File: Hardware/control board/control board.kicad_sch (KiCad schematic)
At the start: 9 parts, among them J1 Conn_01x03_Pin, J2 Conn_01x03_Pin, J3 Conn_01x03_Pin, J4 Conn_01x03_Pin, J5 Conn_01x03_Pin, J6 Conn_01x03_Pin, J7 Conn_01x03_Pin, J8 Conn_01x03_Pin

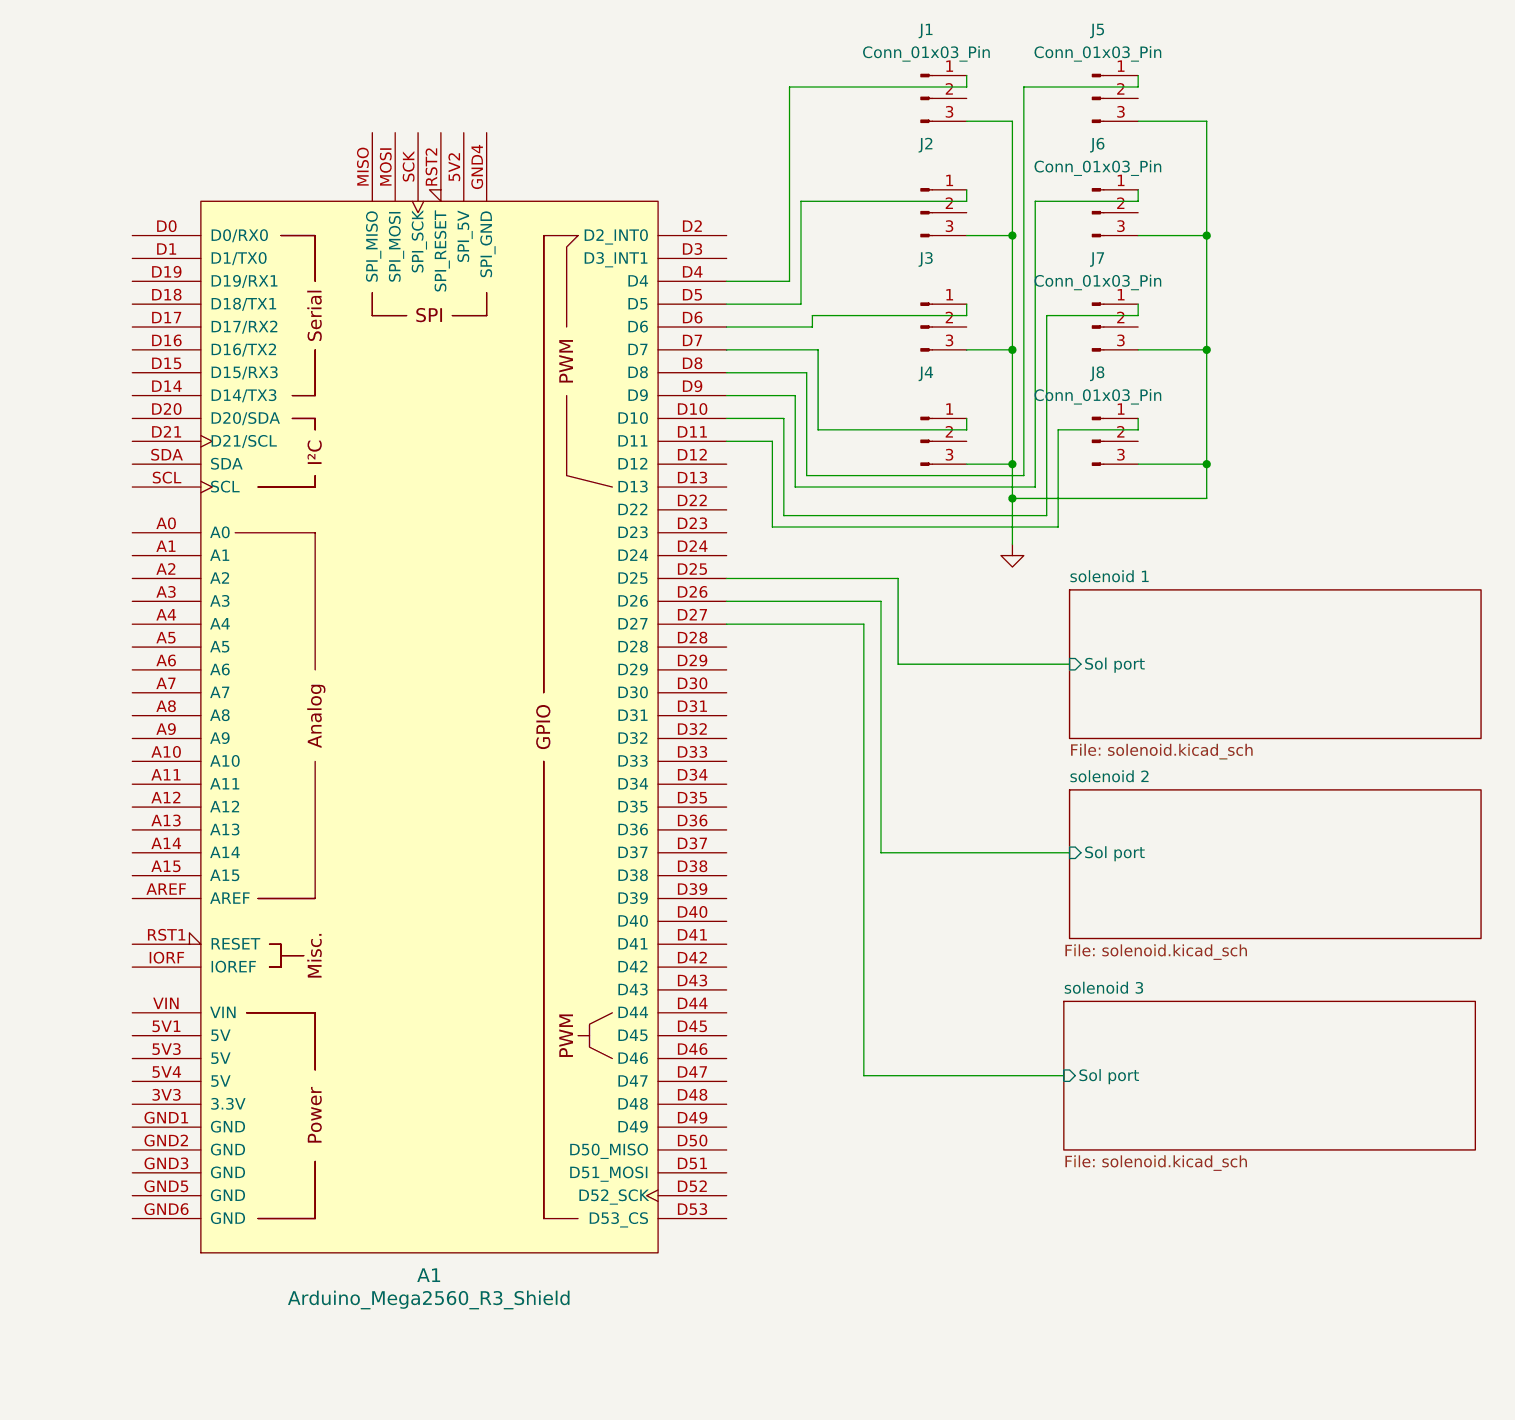
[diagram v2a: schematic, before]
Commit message: updated resistor values for 14.8 V battery
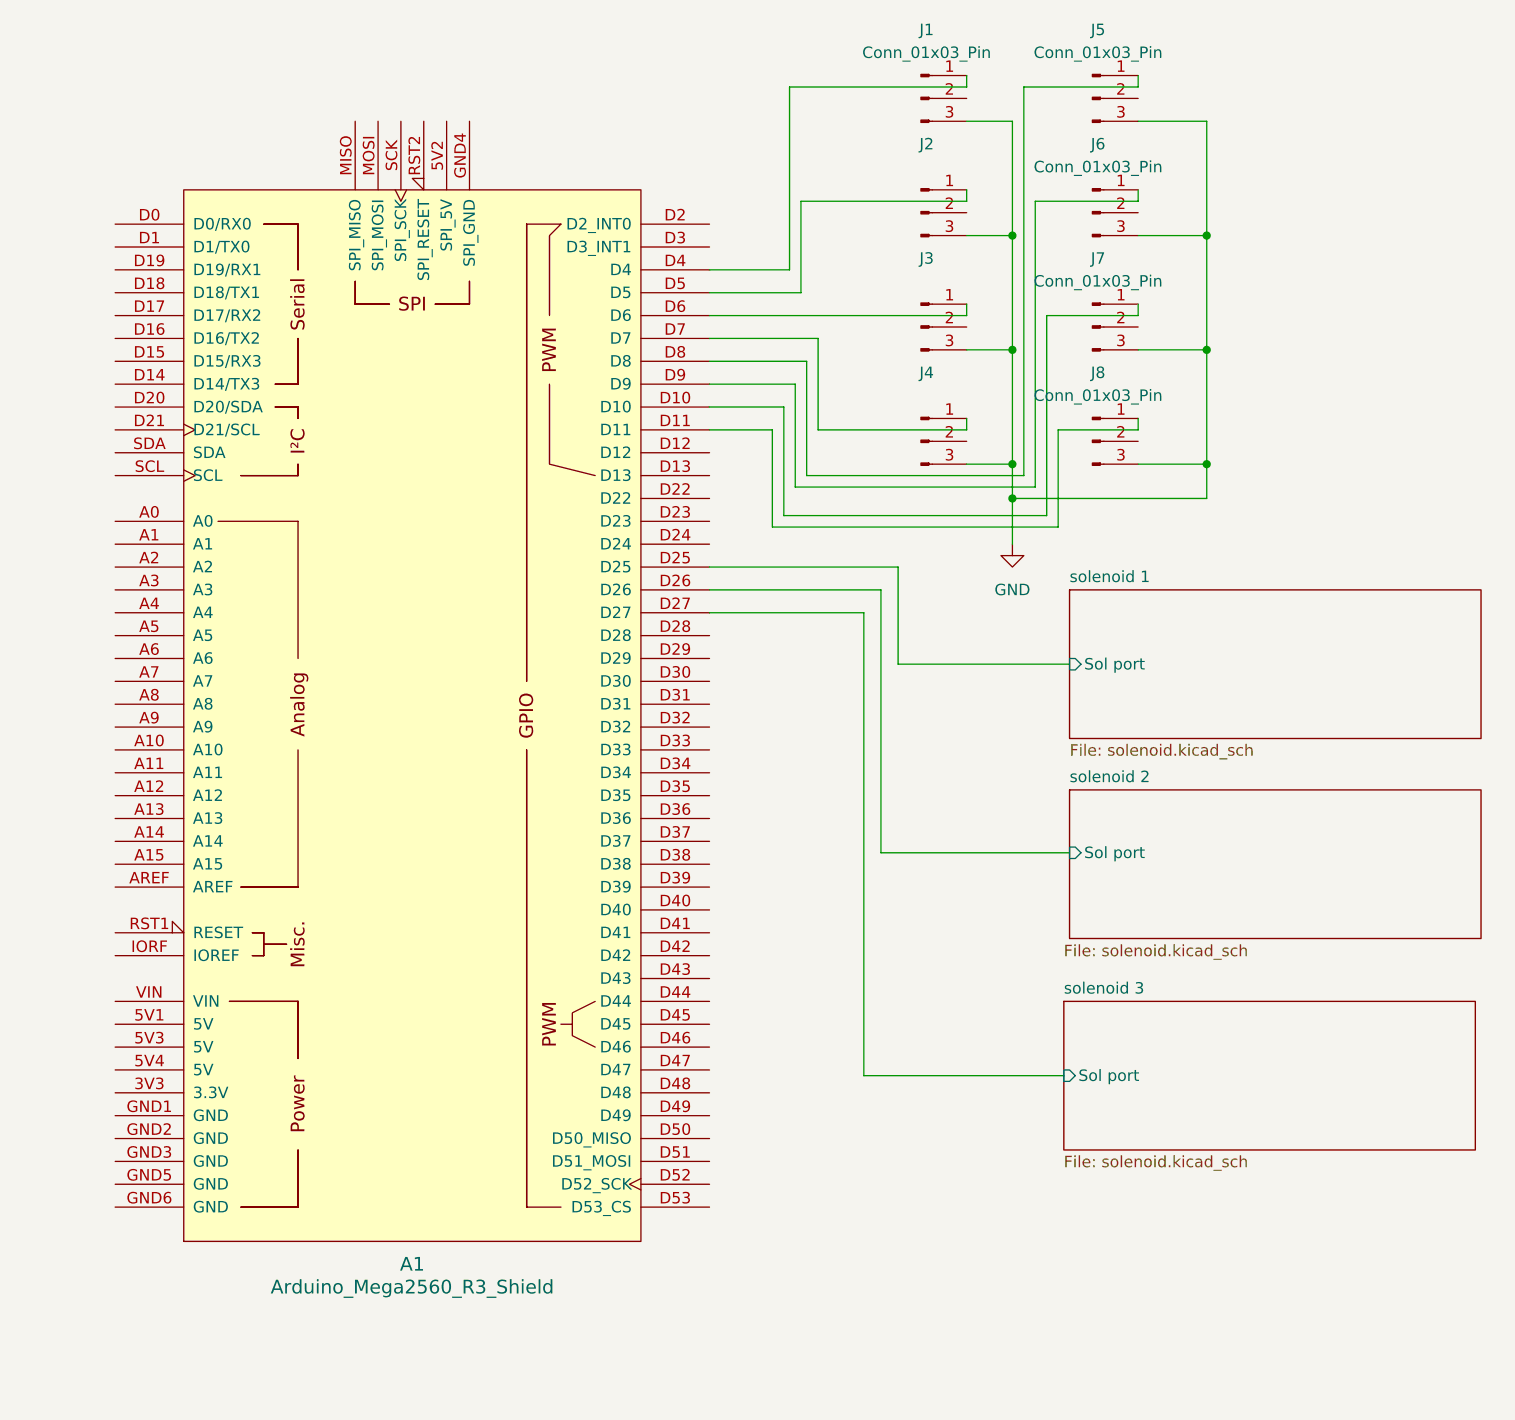
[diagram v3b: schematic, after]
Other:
- moved on the sheet: A1
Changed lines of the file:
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@@
     (stroke (width 0) (type default))
   )
-  (wire (pts (xy 102.87 46.99) (xy 120.015 46.99))
+  (wire (pts (xy 91.44 46.99) (xy 120.015 46.99))
     (stroke (width 0) (type default))
   )
@@
     (stroke (width 0) (type default))
   )
-  (wire (pts (xy 99.695 58.42) (xy 93.345 58.42))
+  (wire (pts (xy 99.695 57.15) (xy 91.44 57.15))
     (stroke (width 0) (type default))
   )
@@
     (stroke (width 0) (type default))
   )
-  (wire (pts (xy 112.395 85.725) (xy 112.395 76.2))
+  (wire (pts (xy 112.395 74.93) (xy 112.395 85.725))
     (stroke (width 0) (type default))
   )
@@
     (stroke (width 0) (type default))
   )
-  (wire (pts (xy 112.395 76.2) (xy 93.345 76.2))
+  (wire (pts (xy 112.395 74.93) (xy 91.44 74.93))
     (stroke (width 0) (type default))
   )
@@
     (stroke (width 0) (type default))
   )
-  (wire (pts (xy 101.6 45.72) (xy 93.345 45.72))
-    (stroke (width 0) (type default))
-  )
-  (wire (pts (xy 102.235 64.77) (xy 102.235 53.34))
-    (stroke (width 0) (type default))
-  )
-  (wire (pts (xy 100.33 21.59) (xy 100.33 43.18))
-    (stroke (width 0) (type default))
-  )
-  (wire (pts (xy 99.695 69.215) (xy 99.695 58.42))
+  (wire (pts (xy 101.6 44.45) (xy 91.44 44.45))
+    (stroke (width 0) (type default))
+  )
+  (wire (pts (xy 102.235 64.77) (xy 102.235 52.07))
+    (stroke (width 0) (type default))
+  )
+  (wire (pts (xy 100.33 41.91) (xy 100.33 21.59))
+    (stroke (width 0) (type default))
+  )
+  (wire (pts (xy 99.695 69.215) (xy 99.695 57.15))
     (stroke (width 0) (type default))
   )
@@
     (stroke (width 0) (type default))
   )
-  (wire (pts (xy 103.505 59.69) (xy 103.505 50.8))
+  (wire (pts (xy 103.505 49.53) (xy 103.505 59.69))
     (stroke (width 0) (type default))
   )
@@
     (stroke (width 0) (type default))
   )
-  (wire (pts (xy 98.425 60.96) (xy 93.345 60.96))
+  (wire (pts (xy 98.425 59.69) (xy 91.44 59.69))
     (stroke (width 0) (type default))
   )
@@
     (stroke (width 0) (type default))
   )
-  (wire (pts (xy 102.235 53.34) (xy 93.345 53.34))
-    (stroke (width 0) (type default))
-  )
-  (wire (pts (xy 108.585 131.445) (xy 108.585 81.28))
+  (wire (pts (xy 102.235 52.07) (xy 91.44 52.07))
+    (stroke (width 0) (type default))
+  )
+  (wire (pts (xy 108.585 131.445) (xy 108.585 80.01))
     (stroke (width 0) (type default))
   )
@@
     (stroke (width 0) (type default))
   )
-  (wire (pts (xy 100.965 66.04) (xy 100.965 55.88))
+  (wire (pts (xy 100.965 66.04) (xy 100.965 54.61))
     (stroke (width 0) (type default))
   )
@@
     (stroke (width 0) (type default))
   )
-  (wire (pts (xy 110.49 78.74) (xy 93.345 78.74))
+  (wire (pts (xy 110.49 77.47) (xy 91.44 77.47))
     (stroke (width 0) (type default))
   )
@@
     (stroke (width 0) (type default))
   )
-  (wire (pts (xy 100.33 43.18) (xy 93.345 43.18))
-    (stroke (width 0) (type default))
-  )
-  (wire (pts (xy 102.87 46.99) (xy 102.87 48.26))
+  (wire (pts (xy 100.33 41.91) (xy 91.44 41.91))
     (stroke (width 0) (type default))
   )
@@
     (stroke (width 0) (type default))
   )
-  (wire (pts (xy 110.49 106.68) (xy 110.49 78.74))
+  (wire (pts (xy 110.49 106.68) (xy 110.49 77.47))
     (stroke (width 0) (type default))
   )
@@
     (stroke (width 0) (type default))
   )
-  (wire (pts (xy 101.6 34.29) (xy 101.6 45.72))
-    (stroke (width 0) (type default))
-  )
-  (wire (pts (xy 103.505 50.8) (xy 93.345 50.8))
-    (stroke (width 0) (type default))
-  )
-  (wire (pts (xy 98.425 70.485) (xy 98.425 60.96))
+  (wire (pts (xy 101.6 44.45) (xy 101.6 34.29))
+    (stroke (width 0) (type default))
+  )
+  (wire (pts (xy 103.505 49.53) (xy 91.44 49.53))
+    (stroke (width 0) (type default))
+  )
+  (wire (pts (xy 98.425 59.69) (xy 98.425 70.485))
     (stroke (width 0) (type default))
   )
@@
     (stroke (width 0) (type default))
   )
-  (wire (pts (xy 108.585 81.28) (xy 93.345 81.28))
-    (stroke (width 0) (type default))
-  )
-  (wire (pts (xy 102.87 48.26) (xy 93.345 48.26))
+  (wire (pts (xy 108.585 80.01) (xy 91.44 80.01))
     (stroke (width 0) (type default))
   )
@@
     (stroke (width 0) (type default))
   )
-  (wire (pts (xy 100.965 55.88) (xy 93.345 55.88))
-    (stroke (width 0) (type default))
-  )
-  (symbol (lib_id "power:GND") (at 125.095 72.39 0) (unit 1)
+  (wire (pts (xy 100.965 54.61) (xy 91.44 54.61))
+    (stroke (width 0) (type default))
+  )
+  (symbol (lib_id "PCM_arduino-library:Arduino_Mega2560_R3_Shield") (at 58.42 91.44 0) (unit 1)
     (in_bom yes) (on_board yes) (dnp no) (fields_autoplaced)
-    (property "Reference" "#PWR01" (at 125.095 78.74 0)
-      (effects (font (size 1.27 1.27)) hide)
-    )
-    (property "Value" "GND" (at 125.095 77.47 0)
-      (effects (font (size 1.27 1.27)) hide)
-    )
-    (property "Footprint" "" (at 125.095 72.39 0)
-      (effects (font (size 1.27 1.27)) hide)
-    )
-    (property "Datasheet" "" (at 125.095 72.39 0)
-      (effects (font (size 1.27 1.27)) hide)
-    )
-    (pin "1")
-    (instances
-      (project "control board"
-        (path "/cf0863a8-7f64-449b-8eb4-3c06c871fb37"
-          (reference "#PWR01") (unit 1)
-        )
-      )
-    )
-  )
-  (symbol (lib_id "PCM_arduino-library:Arduino_Mega2560_R3_Shield") (at 60.325 92.71 0) (unit 1)
-    (in_bom yes) (on_board yes) (dnp no) (fields_autoplaced)
-    (property "Reference" "A1" (at 60.325 153.67 0)
+    (property "Reference" "A1" (at 58.42 152.4 0)
       (effects (font (size 1.524 1.524)))
     )
-    (property "Value" "Arduino_Mega2560_R3_Shield" (at 60.325 156.21 0)
+    (property "Value" "Arduino_Mega2560_R3_Shield" (at 58.42 154.94 0)
       (effects (font (size 1.524 1.524)))
     )
-    (property "Footprint" "PCM_arduino-library:Arduino_Mega2560_R3_Shield" (at 60.325 166.37 0)
+    (property "Footprint" "PCM_arduino-library:Arduino_Mega2560_R3_Shield" (at 58.42 165.1 0)
       (effects (font (size 1.524 1.524)) hide)
     )
-    (property "Datasheet" "https://docs.arduino.cc/hardware/mega-2560" (at 60.325 162.56 0)
+    (property "Datasheet" "https://docs.arduino.cc/hardware/mega-2560" (at 58.42 161.29 0)
       (effects (font (size 1.524 1.524)) hide)
     )
@@
         )
       )
+    )
+  )
+  (symbol (lib_id "power:GND") (at 125.095 72.39 0) (unit 1)
+    (in_bom yes) (on_board yes) (dnp no) (fields_autoplaced)
+    (property "Reference" "#PWR02" (at 125.095 78.74 0)
+      (effects (font (size 1.27 1.27)) hide)
+    )
+    (property "Value" "GND" (at 125.095 77.47 0)
+      (effects (font (size 1.27 1.27)))
+    )
+    (property "Footprint" "" (at 125.095 72.39 0)
+      (effects (font (size 1.27 1.27)) hide)
+    )
+    (property "Datasheet" "" (at 125.095 72.39 0)
+      (effects (font (size 1.27 1.27)) hide)
+    )
+    (pin "1")
+    (instances
+      (project "control board"
+        (path "/cf0863a8-7f64-449b-8eb4-3c06c871fb37"
+          (reference "#PWR02") (unit 1)
+        )
+      )
